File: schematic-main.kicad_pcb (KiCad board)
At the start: 2 copper layers, 100 x 99.9 mm, 124 parts, among them IC1 AD8544ARUZ-REEL, IC2 LM76202QPWPRQ1, J1 Battery, J10 Motor, J2 CAN, J3 V_P, J4 Conn_01x04, J7 C_P, J8 VALVE, J9 PURGE_VALVE, P1 USB_C_Plug_USB2.0, U2 TPS62933, U3 USBLC6-2P6, U4 ESP32-S3FN8, U5 SN65HVD232, U6 DRV8801PWP, Y1 Crystal_GND24

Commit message: Silkscreen
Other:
- board text added: "Fuel Cylinder Unit v1 Bartłomiej Mierzwa 05.03.2024"
- board text added: "HYDROGEN_SENSOR: 1. +5V 2. GND 3. HYDROGEN_SENSOR 4. ADC"
- board text removed: "Fuel Cell Unit v1 Michał Borkowski 05.03.2024"
- board text removed: "HYDROGEN_SENSOR: HYDROGEN_SENSOR ADC +5V GND"

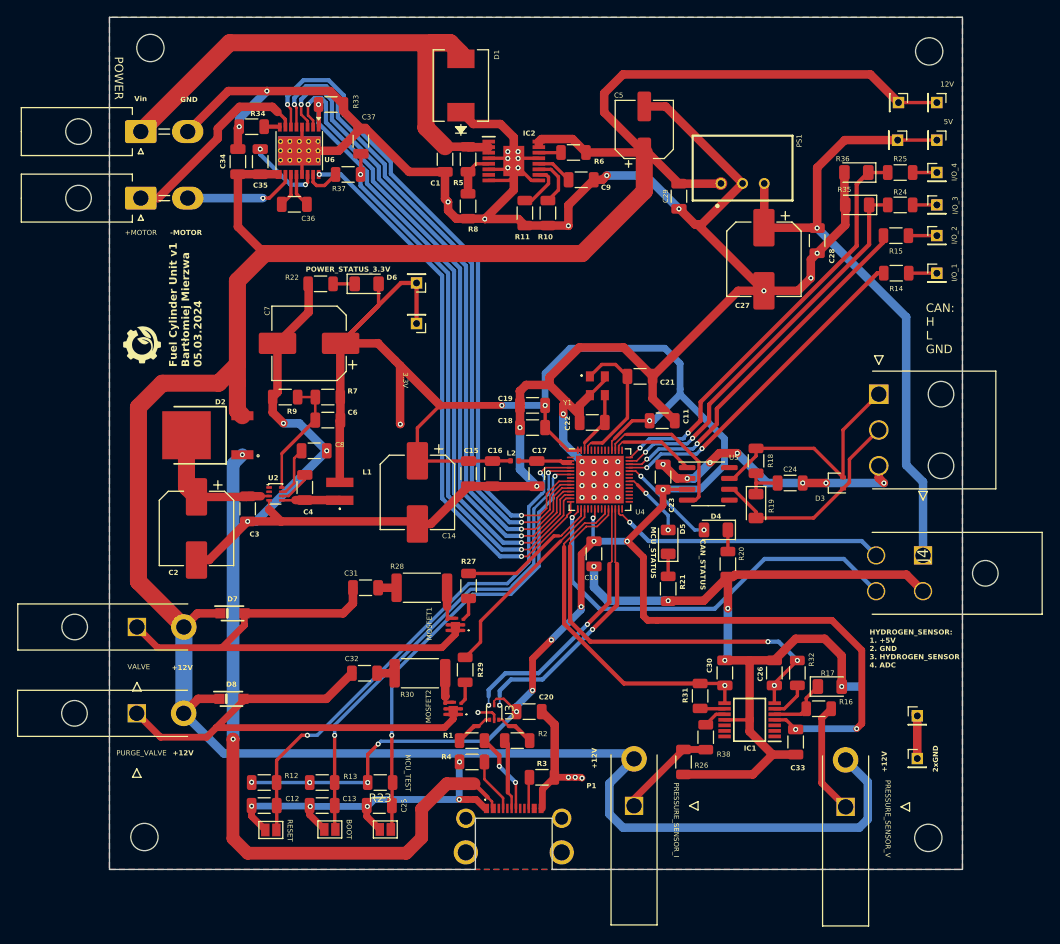
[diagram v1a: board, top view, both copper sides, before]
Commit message: Changing width of mounting holes
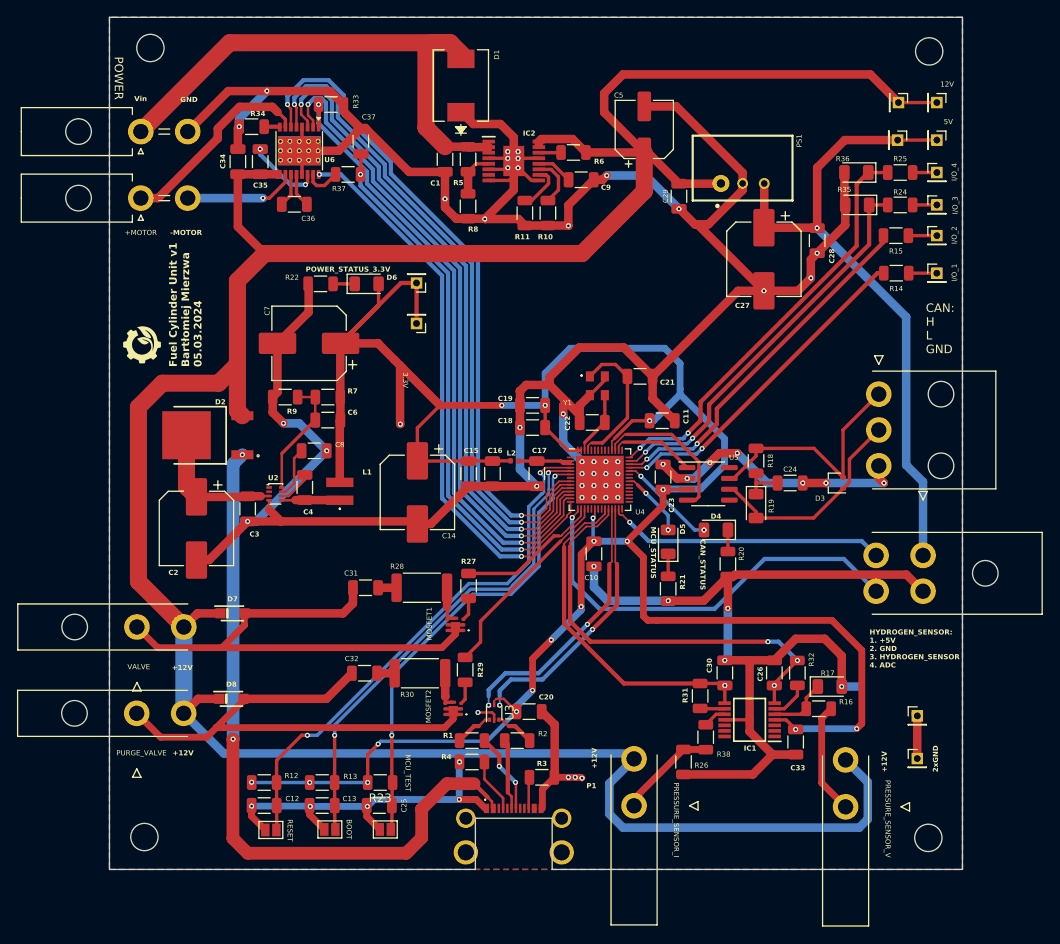
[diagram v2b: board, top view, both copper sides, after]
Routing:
- net GND: track 564.7 -> 565.9 mm
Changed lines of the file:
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@@
 		(pad "1" thru_hole circle
 			(at -2.54 0)
-			(size 1.28 1.28)
-			(drill 0.78)
+			(size 2 2)
+			(drill 1)
 			(layers "*.Cu" "*.Mask")
 			(remove_unused_layers no)
@@
 			(layers "F&B.Cu" "*.Mask")
 		)
-		(pad "1" thru_hole roundrect
+		(pad "1" thru_hole circle
 			(at 0 0 90)
-			(size 2.7 3.7)
+			(size 3 3)
 			(drill 1.8)
 			(layers "*.Cu" "*.Mask")
 			(remove_unused_layers no)
-			(roundrect_rratio 0.092593)
 			(net 97 "/IO_2/+MOTOR")
 			(pinfunction "Pin_1")
 			(pintype "passive")
 		)
-		(pad "2" thru_hole oval
+		(pad "2" thru_hole circle
 			(at 0 5.5 90)
-			(size 2.7 3.7)
+			(size 3 3)
 			(drill 1.8)
 			(layers "*.Cu" "*.Mask")
@@
 			)
 		)
-		(pad "1" thru_hole rect
+		(pad "1" thru_hole circle
 			(at 0 0)
-			(size 2.15 2.15)
+			(size 3 3)
 			(drill 1.8)
 			(layers "*.Cu" "*.Mask")
@@
 			(layers "*.Cu" "*.Mask")
 		)
-		(pad "1" thru_hole rect
+		(pad "1" thru_hole circle
 			(at 0 0 90)
-			(size 2.3 2.3)
+			(size 3 3)
 			(drill 1.8)
 			(layers "*.Cu" "*.Mask")
@@
 		(pad "2" thru_hole circle
 			(at -4.2 0 90)
-			(size 2.3 2.3)
+			(size 3 3)
 			(drill 1.8)
 			(layers "*.Cu" "*.Mask")
@@
 		(pad "3" thru_hole circle
 			(at -8.4 0 90)
-			(size 2.3 2.3)
+			(size 3 3)
 			(drill 1.8)
 			(layers "*.Cu" "*.Mask")
@@
 			(layers "*.Cu" "*.Mask")
 		)
-		(pad "1" thru_hole rect
+		(pad "1" thru_hole circle
 			(at 0 0 270)
-			(size 2.15 2.15)
+			(size 3 3)
 			(drill 1.8)
 			(layers "*.Cu" "*.Mask")
@@
 			)
 		)
-		(pad "1" thru_hole rect
+		(pad "1" thru_hole circle
 			(at 0 0)
-			(size 2.15 2.15)
+			(size 3 3)
 			(drill 1.8)
 			(layers "*.Cu" "*.Mask")
@@
 			(layers "*.Cu" "*.Mask")
 		)
-		(pad "1" thru_hole roundrect
+		(pad "1" thru_hole circle
 			(at 0 0 90)
-			(size 2.7 3.7)
+			(size 3 3)
 			(drill 1.8)
 			(layers "*.Cu" "*.Mask")
 			(remove_unused_layers no)
-			(roundrect_rratio 0.092593)
 			(net 1 "/Power /Vin")
 			(pinfunction "Pin_1")
 			(pintype "passive")
 		)
-		(pad "2" thru_hole oval
+		(pad "2" thru_hole circle
 			(at 0 5.5 90)
-			(size 2.7 3.7)
+			(size 3 3)
 			(drill 1.8)
 			(layers "*.Cu" "*.Mask")
@@
 			(layers "*.Cu" "*.Mask")
 		)
-		(pad "1" thru_hole rect
+		(pad "1" thru_hole circle
 			(at 0 0 270)
-			(size 2.15 2.15)
+			(size 3 3)
 			(drill 1.8)
 			(layers "*.Cu" "*.Mask")
@@
 			(at 0 0 90)
 			(layer "F.SilkS")
+			(hide yes)
 			(effects
 				(font
@@
 			(layers "*.Cu" "*.Mask")
 		)
-		(pad "1" thru_hole rect
+		(pad "1" thru_hole circle
 			(at 0 0 90)
-			(size 2.15 2.15)
+			(size 3 3)
 			(drill 1.8)
 			(layers "*.Cu" "*.Mask")
@@
 		(pad "2" thru_hole circle
 			(at -4.2 0 90)
-			(size 2.15 2.15)
+			(size 3 3)
 			(drill 1.8)
 			(layers "*.Cu" "*.Mask")
@@
 		(pad "3" thru_hole circle
 			(at 0 -5.5 90)
-			(size 2.15 2.15)
+			(size 3 3)
 			(drill 1.8)
 			(layers "*.Cu" "*.Mask")
@@
 		(pad "4" thru_hole circle
 			(at -4.2 -5.5 90)
-			(size 2.15 2.15)
+			(size 3 3)
 			(drill 1.8)
 			(layers "*.Cu" "*.Mask")
@@
 	)
 	(segment
+		(start 117.624198 76.169)
+		(end 119.231 76.169)
+		(width 1)
+		(layer "F.Cu")
+		(net 2)
+	)
+	(segment
 		(start 124.41915 140.6625)
 		(end 126.7457 138.33595)
@@
 	)
 	(segment
-		(start 114.192198 62.35)
-		(end 123.224198 71.382)
-		(width 1)
-		(layer "F.Cu")
-		(net 2)
-	)
-	(segment
 		(start 95.7 69.55)
 		(end 95.7 69.45)
@@
 	)
 	(segment
+		(start 115.45 62.35)
+		(end 123.224198 70.124198)
+		(width 1)
+		(layer "F.Cu")
+		(net 2)
+	)
+	(segment
 		(start 84.8 111)
 		(end 85.1 111.3)
@@
 	)
 	(segment
+		(start 88.338 73.188)
+		(end 88.338 74.188)
+		(width 1)
+		(layer "F.Cu")
+		(net 2)
+	)
+	(segment
 		(start 142.43385 117.24)
 		(end 144.3781 119.18425)
@@
 	)
 	(segment
+		(start 111.7 62.35)
+		(end 115.45 62.35)
+		(width 1)
+		(layer "F.Cu")
+		(net 2)
+	)
+	(segment
 		(start 71.575 70.325)
 		(end 71.575 67.875)
@@
 	)
 	(segment
-		(start 117.624198 76.169)
-		(end 118.437198 76.169)
-		(width 1)
-		(layer "F.Cu")
-		(net 2)
-	)
-	(segment
 		(start 97.125 100)
 		(end 97.125 97.4)
@@
 	)
 	(segment
+		(start 123.224198 72.175802)
+		(end 123.224198 71.382)
+		(width 1)
+		(layer "F.Cu")
+		(net 2)
+	)
+	(segment
 		(start 95.675 68.425)
 		(end 95.7 68.45)
@@
 	)
 	(segment
-		(start 88.338 73.188)
-		(end 88.7 73.55)
+		(start 122.36 117.24)
+		(end 142.43385 117.24)
 		(width 1)
 		(layer "F.Cu")
@@
 	)
 	(segment
-		(start 122.36 117.24)
-		(end 142.43385 117.24)
+		(start 135.26 76.261198)
+		(end 131.964198 79.557)
 		(width 1)
 		(layer "F.Cu")
@@
 	)
 	(segment
-		(start 135.26 76.261198)
-		(end 131.964198 79.557)
+		(start 89.6625 75.5125)
+		(end 91.038 75.5125)
 		(width 1)
 		(layer "F.Cu")
@@
 	)
 	(segment
-		(start 88.7 73.55)
-		(end 88.7 74.55)
-		(width 1)
-		(layer "F.Cu")
-		(net 2)
-	)
-	(segment
 		(start 120.5 103)
 		(end 119.4 104.1)
@@
 	)
 	(segment
-		(start 111.7 62.35)
-		(end 114.192198 62.35)
-		(width 1)
-		(layer "F.Cu")
-		(net 2)
-	)
-	(segment
 		(start 59.2 115.525)
 		(end 60.675 115.525)
@@
 	)
 	(segment
-		(start 89.6625 75.5125)
-		(end 91.038 75.5125)
-		(width 1)
-		(layer "F.Cu")
-		(net 2)
-	)
-	(segment
 		(start 102.2 97.4)
 		(end 102.2 98.4)
@@
 	)
 	(segment
+		(start 123.224198 70.124198)
+		(end 123.224198 71.382)
+		(width 1)
+		(layer "F.Cu")
+		(net 2)
+	)
+	(segment
 		(start 125.724198 83.969)
 		(end 129.724198 83.969)
@@
 	)
 	(segment
+		(start 88.338 74.188)
+		(end 89.6625 75.5125)
+		(width 1)
+		(layer "F.Cu")
+		(net 2)
+	)
+	(segment
 		(start 72.4625 144.3375)
 		(end 72.5375 144.4125)
@@
 	)
 	(segment
-		(start 88.7 74.55)
-		(end 89.6625 75.5125)
-		(width 1)
-		(layer "F.Cu")
-		(net 2)
-	)
-	(segment
 		(start 91.643892 64.4132)
 		(end 94.8382 64.4132)
@@
 	)
 	(segment
-		(start 118.437198 76.169)
-		(end 123.224198 71.382)
-		(width 1)
-		(layer "F.Cu")
-		(net 2)
-	)
-	(segment
 		(start 101.1625 141)
 		(end 102.8 141)
@@
 	)
 	(segment
+		(start 119.231 76.169)
+		(end 123.224198 72.175802)
+		(width 1)
+		(layer "F.Cu")
+		(net 2)
+	)
+	(segment
 		(start 104.125 98.525)
 		(end 104.125 99.4)
@@
 	)
 	(via
-		(at 88.7 73.55)
+		(at 88.338 73.188)
 		(size 0.6)
 		(drill 0.3)

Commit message: Change presure sensor socket
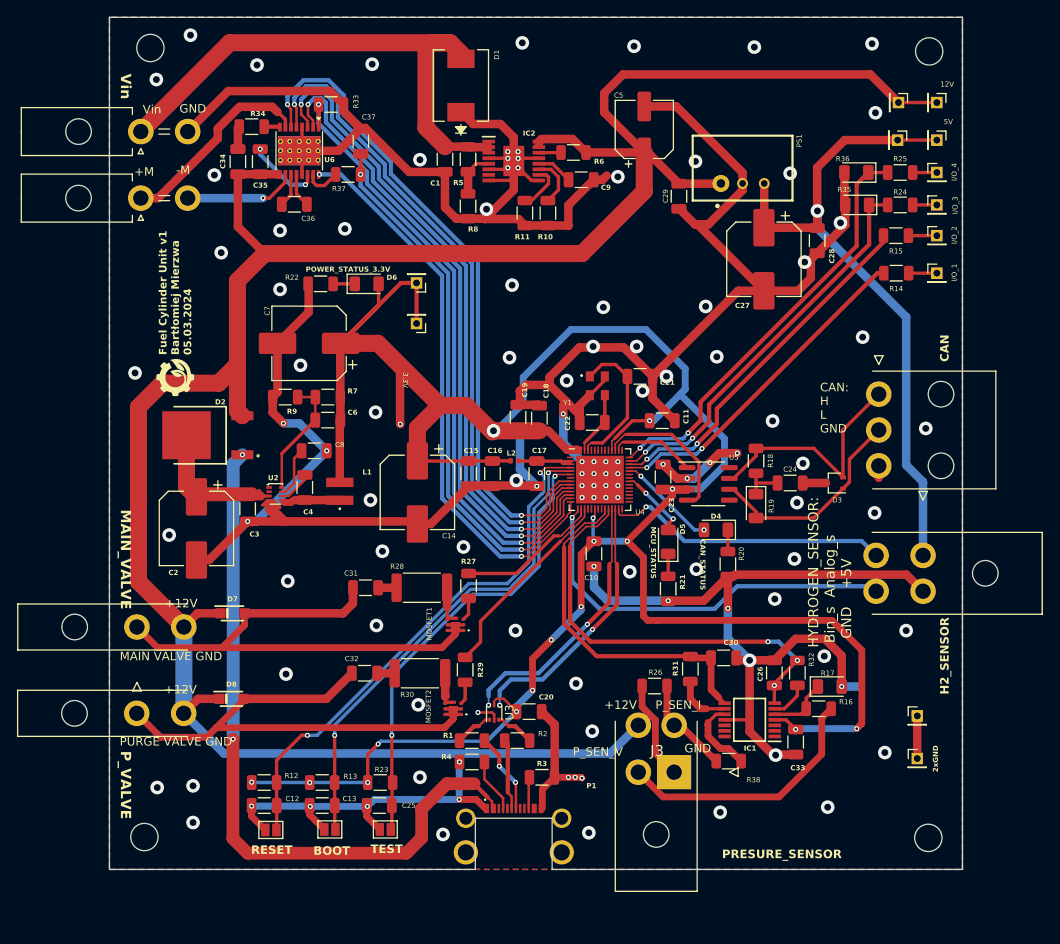
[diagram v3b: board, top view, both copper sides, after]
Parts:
- removed J7: C_P, Connector_Molex:39-30-102Y
- J10: value Motor -> Battery
- J3: footprint Connector_Molex:39-30-102Y -> Lib:39-30-104Y
- moved J3 20.5 mm to (115.2, 140.4)
- moved R26 9.53 mm to (112.9, 130.3), turned to 0 degrees
- moved R38 3.89 mm to (121.6, 139.1), turned to 0 degrees
- moved R31 3.36 mm to (117.1, 128.3)
- moved C19 2.20 mm to (96.9, 98.8), turned to 90 degrees
- moved C30 1.77 mm to (121.0, 127.0), turned to 0 degrees
- moved C18 1.36 mm to (99.4, 98.9), turned to 90 degrees
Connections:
- J10 pad 1: /IO_2/+MOTOR -> (no net)
- J10 pad 2: /IO_2/-MOTOR -> (no net)
- J3 pad 1: /IO/PRESSURE_SENSOR_V -> GND
- J3 pad 2: +12V -> /IO/PRESSURE_SENSOR_V
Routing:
- net +12V: track 325.9 -> 280.4 mm
- net GND: track 565.9 -> 540.5 mm, vias 59 -> 113
- net /IO/PRESSURE_SENSOR_V: track 13.1 -> 30.6 mm
- net +3.3V: track 296.8 -> 311.4 mm, vias 18 -> 17
- net Net-(U2-VIN): track 17.2 -> 27.2 mm
- net Net-(IC1-+IN_C): track 2.72 -> 9.42 mm
- net Net-(IC1--IN_C): track 2.88 -> 6.51 mm
- net Net-(U2-SW): track 6.82 -> 9.72 mm
- net /HYDROGEN_SENSOR_ADC: track 49.7 -> 47.1 mm
- net +5V: track 77.4 -> 79.5 mm
- net /PRESSURE_SENSOR_I_MCU: track 40.2 -> 41.2 mm, vias 1 -> 0
- net /HYDROGEN_SENSOR_: track 32.7 -> 33.6 mm
- net /IO/LED_MCU_STATUS: track 7.92 -> 8.53 mm
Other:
- board text added: "+M"
- board text added: "-M"
- board text added: "CAN"
- board text added: "H2_SENSOR"
- board text added: "HYDROGEN_SENSOR: Bin_s Analog_s GND +5V"
- board text added: "MAIN VALVE GND"
- board text added: "MAIN_VALVE"
- board text added: "PRESURE_SENSOR"
- board text added: "PURGE VALVE GND"
- board text added: "P_SEN_I"
- board text added: "P_SEN_V"
- board text added: "P_VALVE"
- board text added: "TEST"
- board text removed: "+MOTOR"
- board text removed: "-MOTOR"
- board text removed: "HYDROGEN_SENSOR: 1. +5V 2. GND 3. HYDROGEN_SENSOR 4. ADC"
- board text removed: "MCU_TEST"
- board text removed: "POWER"
- board text removed: "PRESSURE_SENSOR_I"
- board text removed: "PRESSURE_SENSOR_V"
- board text removed: "PURGE_VALVE"
- board text removed: "VALVE"
